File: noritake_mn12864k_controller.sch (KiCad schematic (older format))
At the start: 63 parts, among them J1 Conn_01x11, J2 USB_C_Receptacle_USB2.0, J3 TagConnect_TC2030_SWD, J4 Conn_01x18, U10 SRV05-4, U11 SRV05-4, U12 SRV05-4, U2 74HC14, U3 CD4051B, U5 STM32F730R8T6, U8 SRV05-4, U9 XC6206PxxxMR

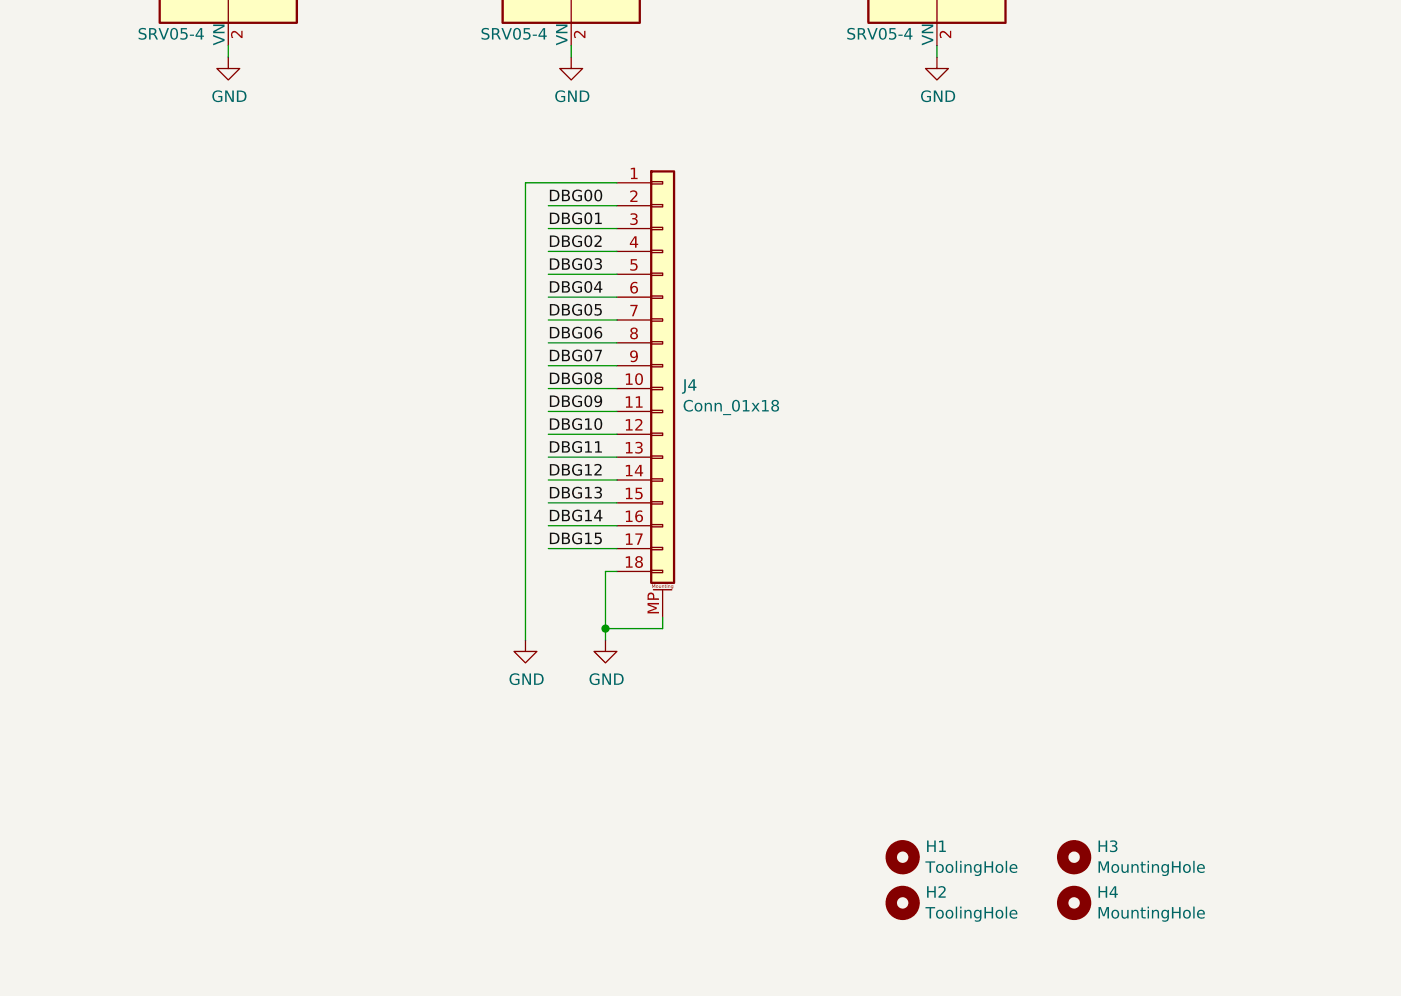
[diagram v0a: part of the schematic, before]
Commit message: Add more VFD VDD2 bypassing
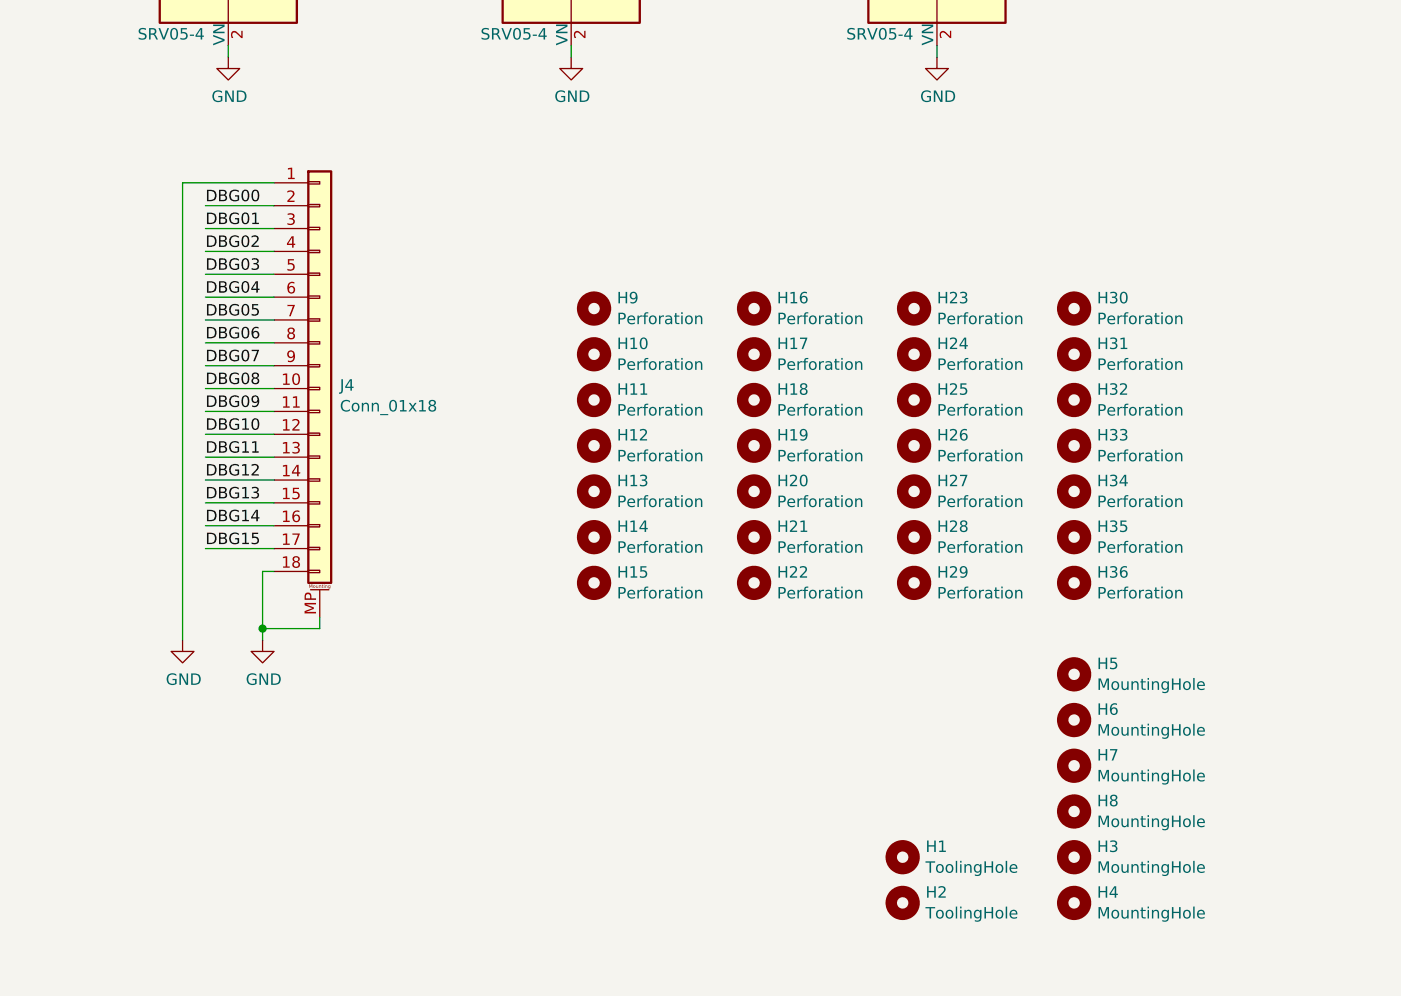
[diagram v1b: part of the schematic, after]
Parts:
- added H10, H11, H12, H13, H14, H15, H16, H17, H18, H19, H20, H21, H22, H23, H24, H25, H26, H27, H28, H29, H30, H31, H32, H33, H34, H35, H36, H9: Perforation, Perforation:Perforation_0.4mm, symbol Mechanical:MountingHole
- added H5, H6, H7, H8: MountingHole, MountingHole:MountingHole_3.2mm_M3, symbol Mechanical:MountingHole
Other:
- moved on the sheet: J4

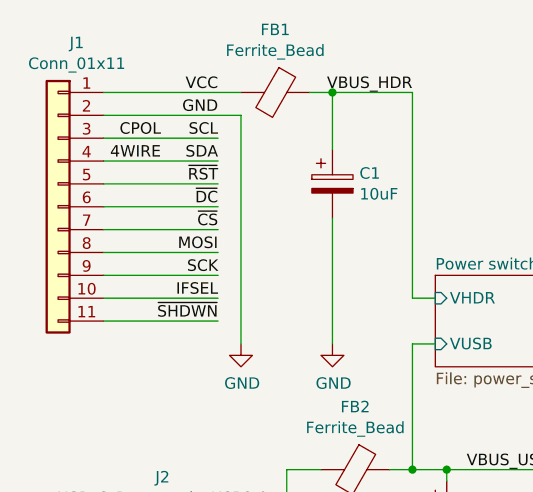
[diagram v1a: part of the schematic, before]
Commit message: Add i2c address select pin
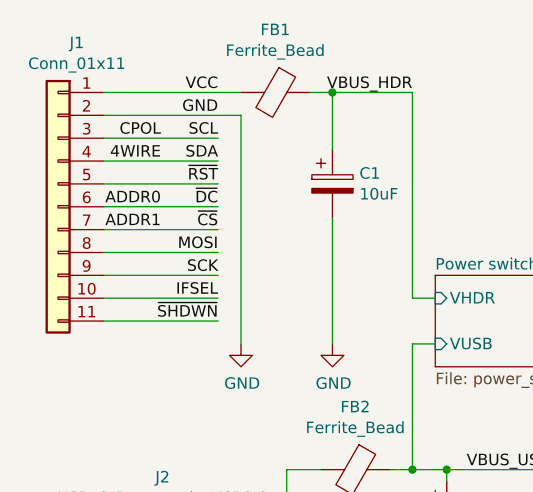
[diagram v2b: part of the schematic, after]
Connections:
- net ~CS renamed ADDR1
- net ~DC renamed ADDR0
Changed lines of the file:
@@
 	1    0    0    -1
 $EndComp
+Text Label 1300 1400 2    50   ~ 0
+ADDR0
+Text Label 1300 1500 2    50   ~ 0
+ADDR1
 $EndSCHEMATC
